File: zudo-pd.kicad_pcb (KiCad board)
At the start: 2 copper layers, 76 x 99 mm, 82 parts, among them J1 USB-C, J2 2541WR-2X08P, J3 2541WR-2X08P, J4 2541WR-2X08P, J5 2541WR-2X08P, J6 1217754-1, J7 1217754-1, J8 1217754-1, J9 1217754-1, U1 CH224D, U2 LM2596S-ADJ, U3 LM2596S-ADJ, U4 LM2596S-ADJ, U6 L7812CD2T-TR, U7 L7805ABD2T-TR, U8 CJ7912_C94173

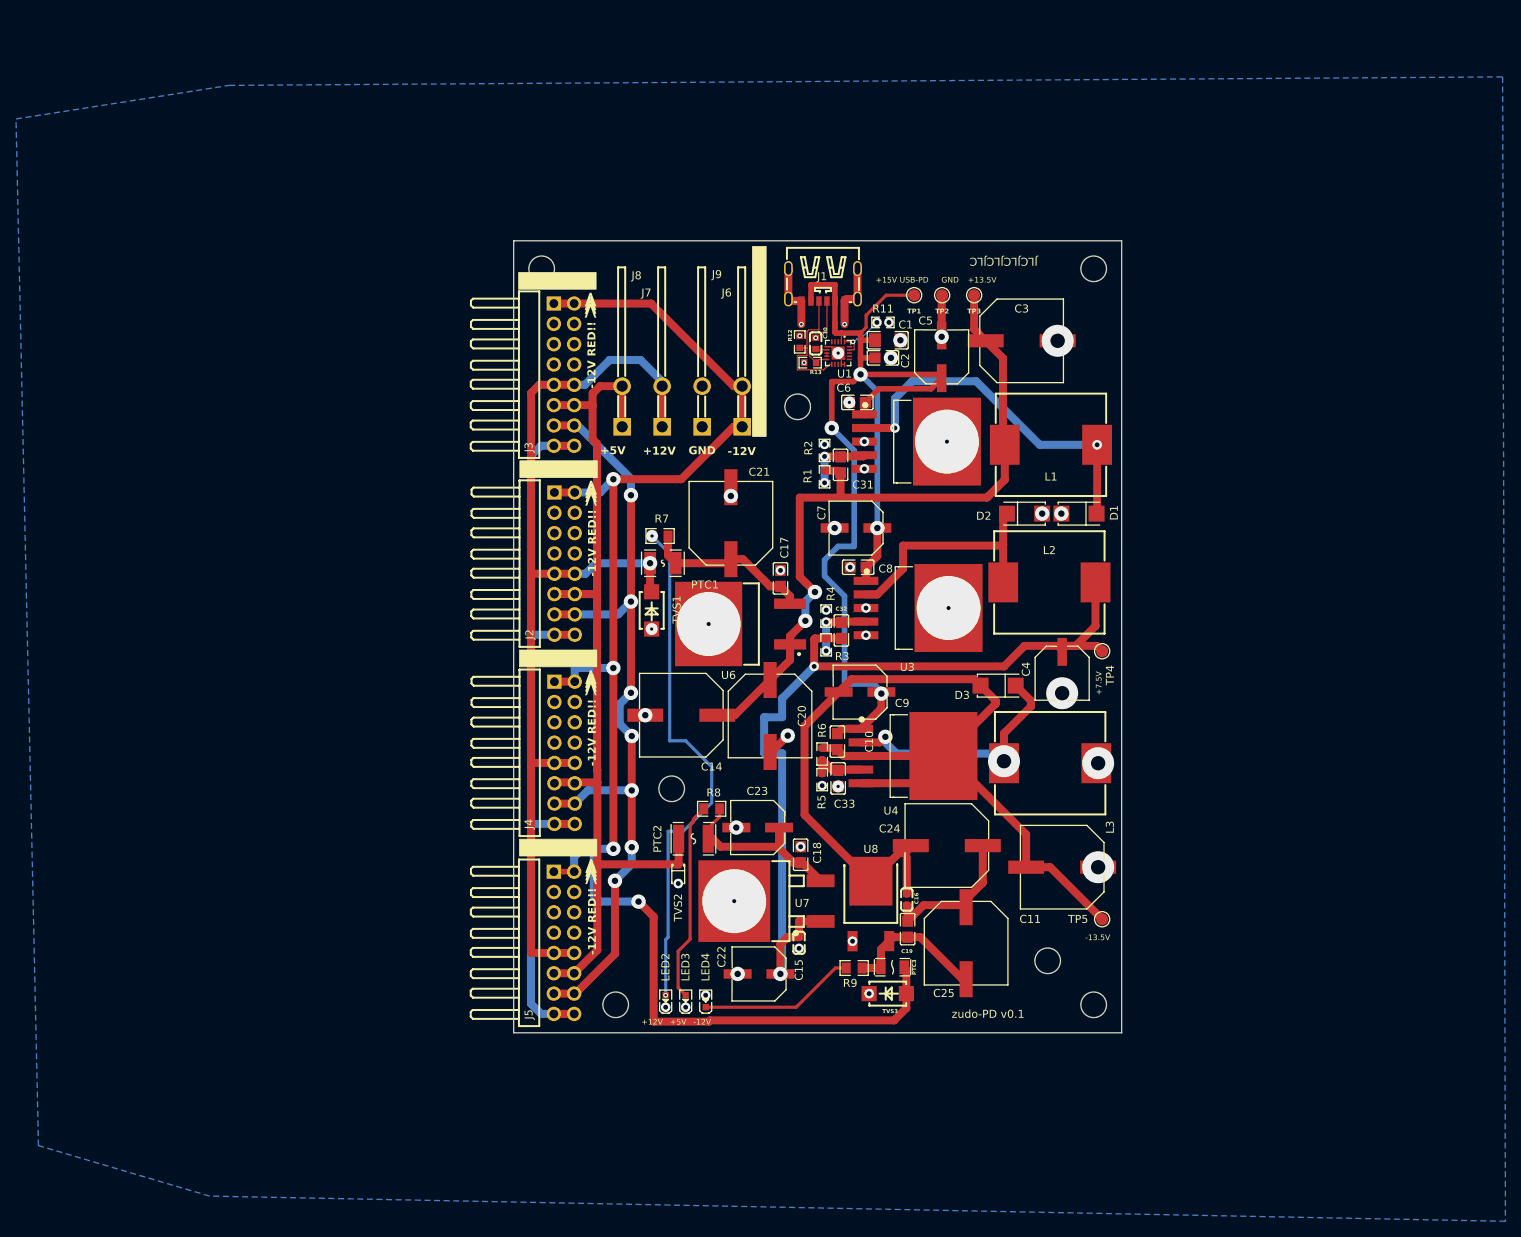
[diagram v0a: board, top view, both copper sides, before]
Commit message: Improve PCB layout for JLCPCB v1.1 production
- Fix via-in-pad issues for small passive components
- Add thermal via arrays under IC thermal pads
- Update trace widths to 0.7mm for 3A USB-PD input paths
- Adjust component placements and routing
- Remove unused output schematic elements

Co-Authored-By: Claude Opus 4.5 <noreply@anthropic.com>
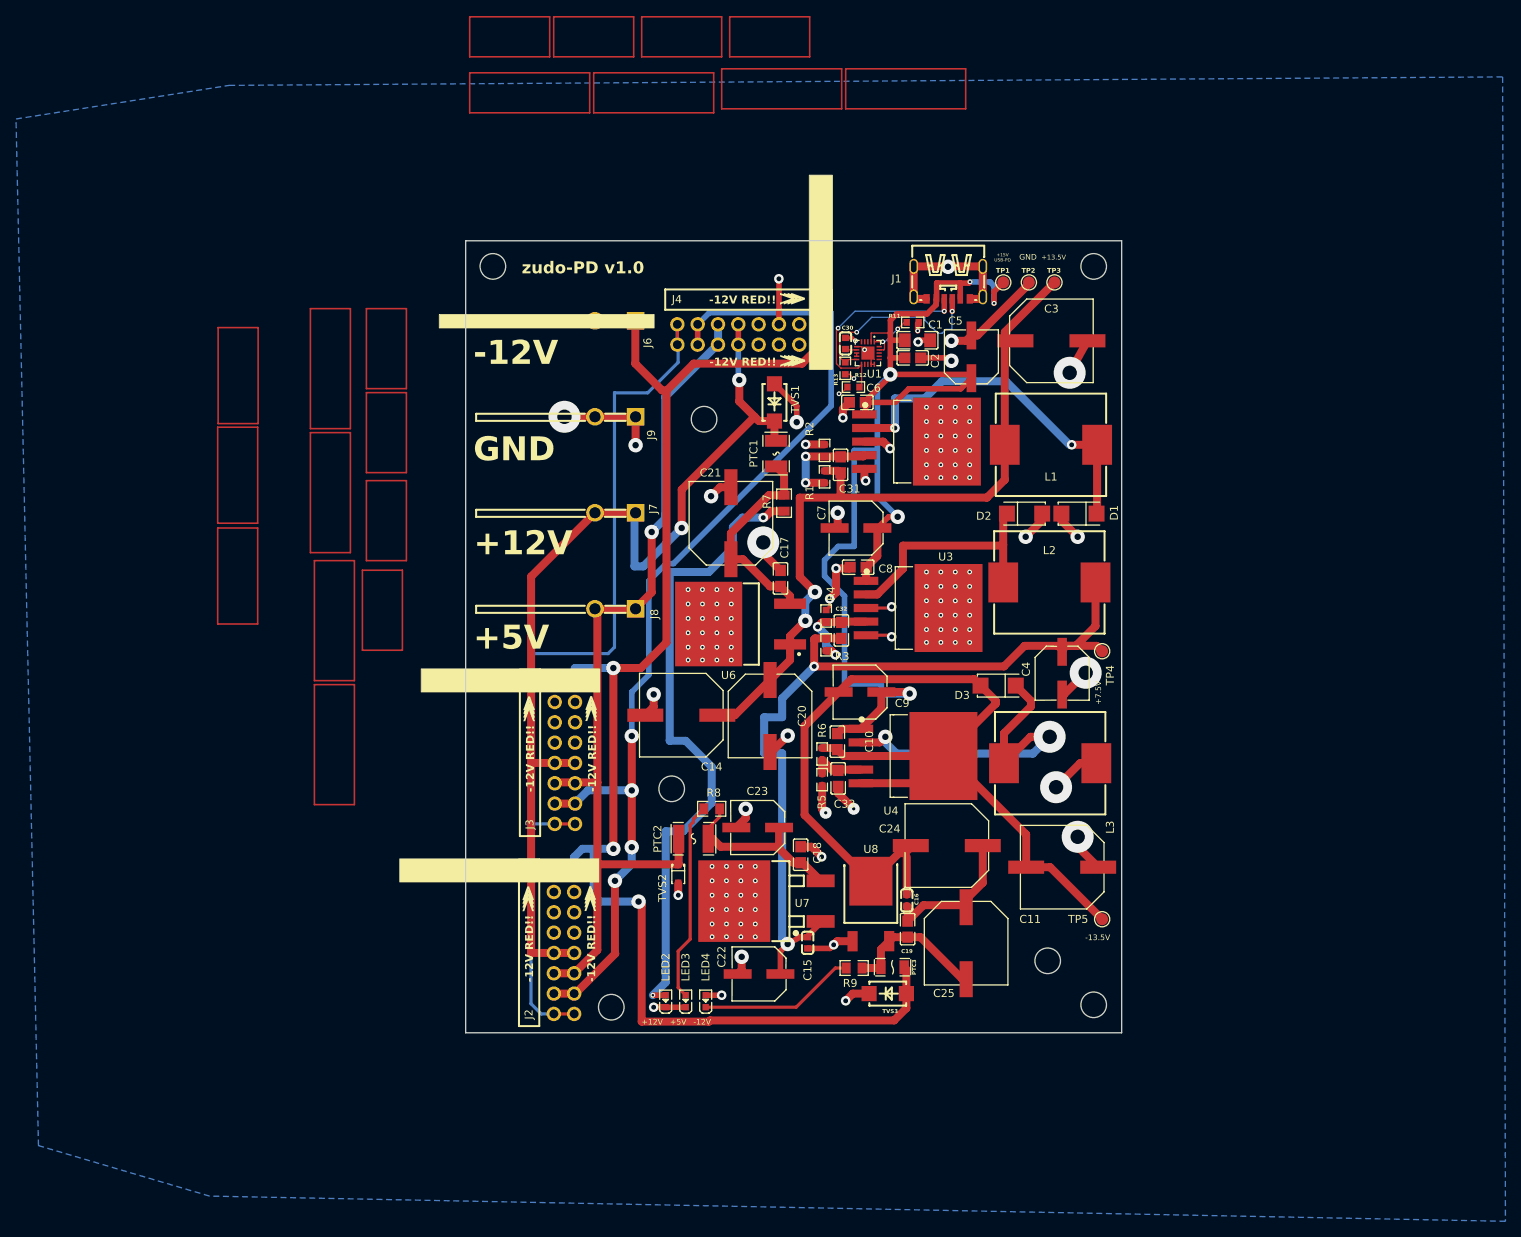
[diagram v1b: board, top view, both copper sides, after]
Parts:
- removed the J2 at (6.36, 40.4)
- removed the REF** at (12.8, 95.5)
- added ?: , , F.Cu at (12.2, 95.8)
- moved J4 57.1 mm to (29.4, 11.7), turned to 180 degrees
- moved J3 47.3 mm to (6.40, 64.0)
- moved TVS1 30.2 mm to (32.6, 20.2), turned to 90 degrees
- moved J8 25.3 mm to (12.7, 46.0), turned to -90 degrees
- moved PTC1 19.7 mm to (32.8, 26.6), turned to 90 degrees
- moved J6 19.1 mm to (12.7, 10.0), turned to -90 degrees
- moved R7 16.0 mm to (33.8, 32.8), turned to -90 degrees
- moved J1 15.7 mm to (54.3, 5.23)
- moved J7 14.5 mm to (12.7, 34.0), turned to -90 degrees
- moved REF** 11.8 mm to (23.8, 22.3)
- moved TP1 11.3 mm to (61.2, 5.20)
- moved TP2 11.0 mm to (64.4, 5.20)
- moved J9 10.9 mm to (12.7, 22.0), turned to -90 degrees
- moved TP3 10.2 mm to (67.6, 5.20)
- moved R12 8.78 mm to (42.5, 18.3), turned to 0 degrees
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- renumbered J5 to J2
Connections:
- net GND rail renamed GND
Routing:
- net GND: track 30.5 -> 172.8 mm, vias 46 -> 138
- net CV rail: track 104.6 -> 132.2 mm, vias 7 -> 4
- net GATE rail: track 91.4 -> 114.5 mm
- net Net-(LED2-A): track 65.1 -> 81.0 mm
- net Net-(J1-CC1): track 11.7 -> 25.4 mm, vias 0 -> 2
- net Net-(D3-K): track 32.3 -> 45.4 mm
- net +15V -> +13.5V gen: track 144.6 -> 156.3 mm, vias 4 -> 5
- net Net-(J1-CC2): track 16.7 -> 26.8 mm, vias 0 -> 2
- net /DC-DC Conversion/+7.5V OUT: track 111.4 -> 105.8 mm
- net Net-(U6-OUT): track 21.2 -> 26.2 mm
- net Net-(U2-Feedback): track 8.34 -> 13.1 mm
- net Net-(U3-Feedback): track 8.64 -> 12.1 mm
- net -12V rail: track 190.0 -> 186.6 mm, vias 4 -> 3
- net /DC-DC Conversion/+13.5V OUT: track 91.7 -> 94.6 mm
- net +5V rail: track 114.7 -> 113.0 mm, vias 0 -> 1
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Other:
- board size 76 x 99 mm -> 82 x 99 mm
- board text added: "< 6mm > pin legth"
- board text added: "zudo-PD v1.0"
- board text removed: "-12V RED!!"
- board text removed: ">"
- board text removed: "JLCJLCJLCJLC"
- board text removed: "zudo-PD v0.1"

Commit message: feat: Update PCB layout with improved routing and net naming
- Sync schematic changes to PCB layout with USBLC6-2SC6 component
- Update output connector designators to J10, J11
- Refine net naming for better clarity
- Update position files output path in project settings

Co-Authored-By: Claude <noreply@anthropic.com>
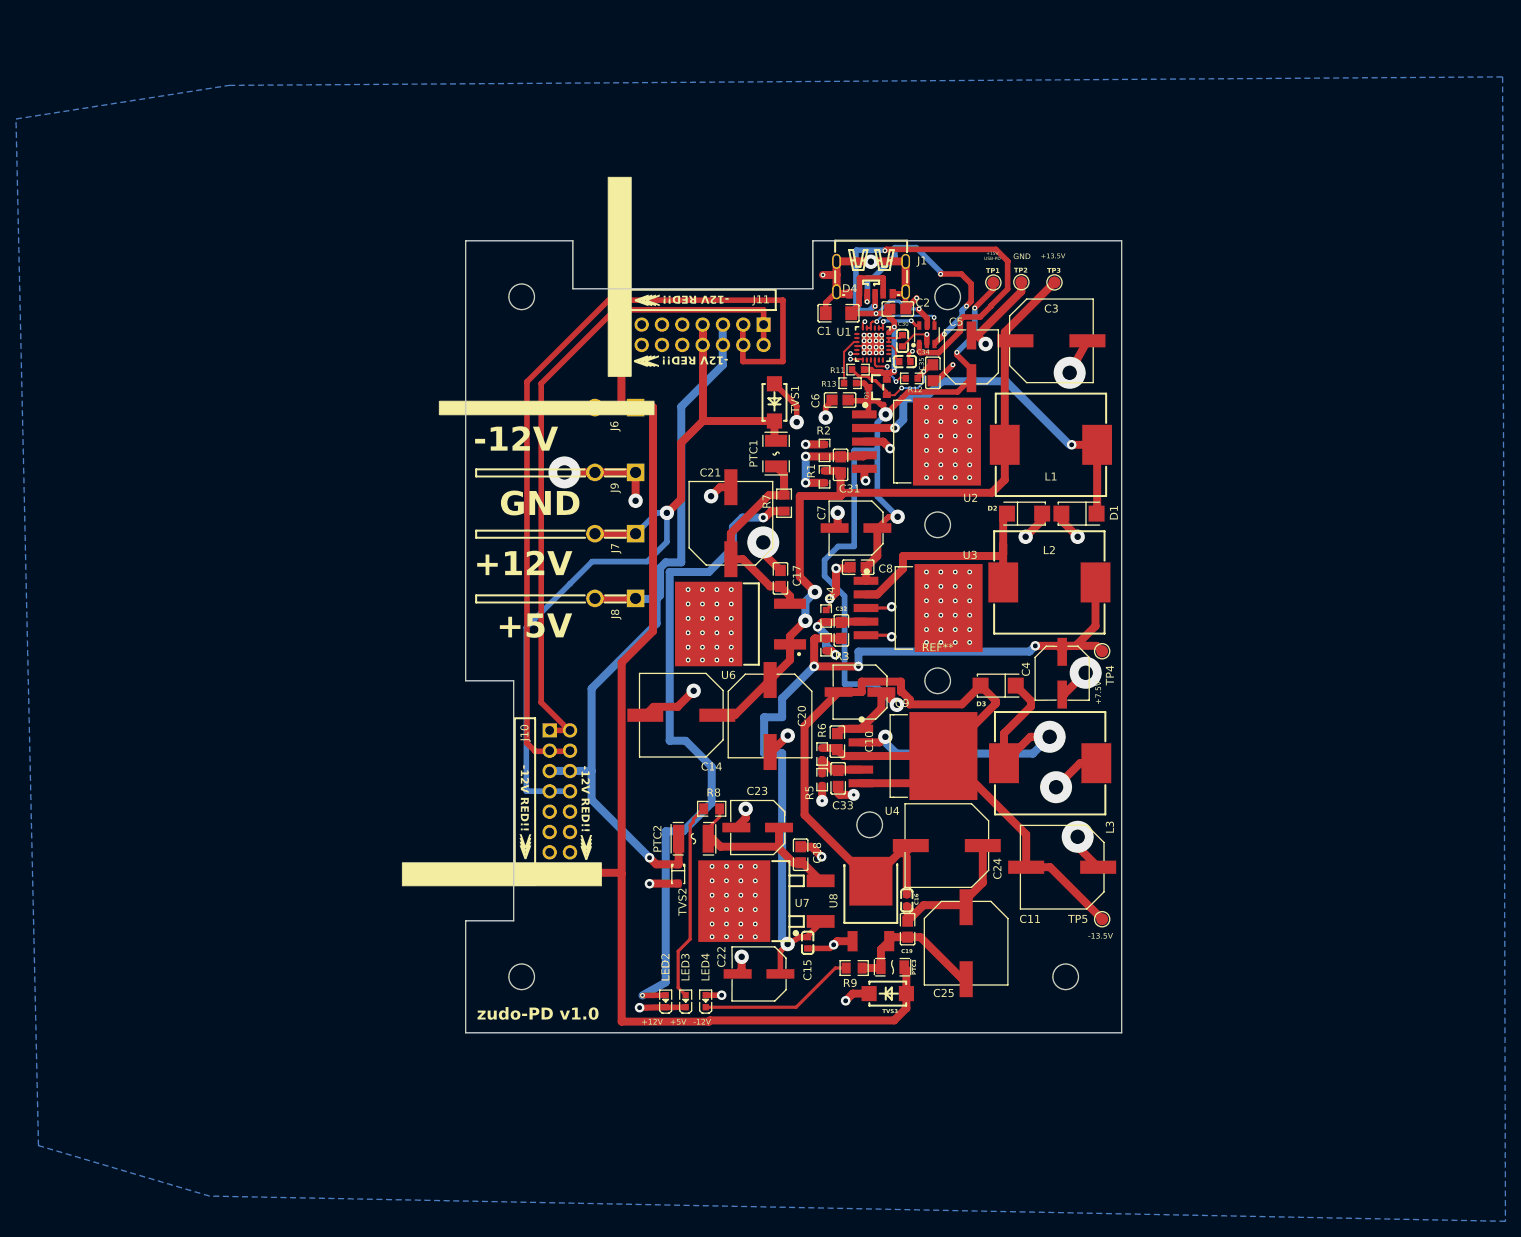
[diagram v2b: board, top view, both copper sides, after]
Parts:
- removed ?: , 
- removed J3, J4: 2541WR-2X08P, zudo-pd:HDR-TH_16P-P2.54-H-M-R2-C8-S2.54
- removed the REF** at (72.5, 3.20)
- removed the REF** at (-2.60, 3.20)
- removed the REF** at (23.8, 22.3)
- removed the REF** at (72.5, 95.5)
- removed the REF** at (66.8, 90.0)
- removed the REF** at (19.8, 68.5)
- added C34: 1uF 16V, zudo-pd:C0603, F.Cu at (48.9, 15.1)
- added C35: 100nF 50V, zudo-pd:C0805, F.Cu at (52.4, 16.5)
- added D4: USBLC6-2SC6, zudo-pd:SOT-23-6_L2.9-W1.6-P0.95-LS2.8-BL, F.Cu at (51.6, 11.8)
- added J11: 2541WR-2X08P, zudo-pd:HDR-TH_16P-P2.54-H-M-R2-C8-S2.54, F.Cu at (22.4, 11.7)
- added Q1: -30V -4A, zudo-pd:SOT-23_L2.9-W1.3-P1.90-LS2.4-BR, F.Cu at (45.5, 18.3)
- added REF**: MountingHole_3.2mm_M3, MountingHole:MountingHole_3.2mm_M3, F.Cu at (1.00, 92.0)
- added REF**: MountingHole_3.2mm_M3, MountingHole:MountingHole_3.2mm_M3, F.Cu at (54.2, 7.00)
- added REF**: MountingHole_3.2mm_M3, MountingHole:MountingHole_3.2mm_M3, F.Cu at (44.5, 73.0)
- added REF**: MountingHole_3.2mm_M3, MountingHole:MountingHole_3.2mm_M3, F.Cu at (1.00, 7.00)
- added REF**: MountingHole_3.2mm_M3, MountingHole:MountingHole_3.2mm_M3, F.Cu at (69.0, 92.0)
- added REF**: MountingHole_3.2mm_M3, MountingHole:MountingHole_3.2mm_M3, F.Cu at (53.0, 55.0)
- added REF**: MountingHole_3.2mm_M3, MountingHole:MountingHole_3.2mm_M3, F.Cu at (53.0, 35.5)
- C30: value 1uF -> 1uF 16V
- R11: value 56k -> 100k
- R12: value 5.1k -> 56k
- R13: value 5.1k -> 470
- U1: value CH224D -> STUSB4500QTR; footprint zudo-pd:QFN-20_L3.0-W3.0-P0.40-BL-EP1.7 -> zudo-pd:QFN-24_L4.0-W4.0-P0.50-BL-EP2.8
- moved J10 17.7 mm to (5.77, 70.1)
- moved J6 10.9 mm to (12.7, 20.9)
- moved C1 10.4 mm to (40.6, 9.05), turned to 0 degrees
- moved J1 9.66 mm to (44.7, 4.60)
- moved R11 9.02 mm to (43.0, 16.1)
- moved R12 7.36 mm to (49.8, 17.2)
- moved C30 7.13 mm to (48.6, 12.5), turned to -90 degrees
- moved J9 6.95 mm to (12.7, 28.9)
- moved C2 6.39 mm to (48.0, 8.52)
- moved J7 2.61 mm to (12.7, 36.6)
- moved C6 2.18 mm to (40.8, 19.9)
- moved R13 1.95 mm to (42.0, 17.8), turned to 180 degrees
- moved J8 1.30 mm to (12.7, 44.7)
- moved U1 1.29 mm to (44.9, 12.9)
- moved TP1 1.24 mm to (60.0, 5.22)
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- renumbered J2 to J10
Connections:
- C1 pad 1: GND -> GND rail
- C1 pad 2: +15V -> +13.5V gen -> VBUS_IN
- C11 pad 1: GND -> GND rail
- C14 pad 2: GND -> GND rail
- C15 pad 2: GND -> GND rail
- C17 pad 1: GND -> GND rail
- C18 pad 2: GND -> GND rail
- C2 pad 1: GND -> GND rail
- C2 pad 2: +15V -> +13.5V gen -> VBUS_IN
- C20 pad 2: GND -> GND rail
- C21 pad 2: GND -> GND rail
- C22 pad 2: GND -> GND rail
- C23 pad 2: GND -> GND rail
- C3 pad 2: GND -> GND rail
- C30 pad 1: Net-(U1-VDD) -> Net-(U1-VREG_2V7)
- C30 pad 2: GND -> GND rail
- C33 pad 1: GND -> GND rail
- C4 pad 2: GND -> GND rail
- C5 pad 2: GND -> GND rail
- C6 pad 2: GND -> GND rail
- C7 pad 2: GND -> GND rail
- C8 pad 2: GND -> GND rail
- D1 pad 2: GND -> GND rail
- D2 pad 2: GND -> GND rail
- J1 pad 7: GND -> GND rail
- J1 pad A12: GND -> GND rail
- J1 pad A9: +15V -> +13.5V gen -> VBUS_IN
- J1 pad B12: GND -> GND rail
- J1 pad B9: +15V -> +13.5V gen -> VBUS_IN
- J10 pad 1: -12V rail -> GATE rail
- J10 pad 10: +12V rail -> GND rail
- J10 pad 11: +5V rail -> GND rail
- J10 pad 12: +5V rail -> GND rail
- J10 pad 13: CV rail -> GND rail
- J10 pad 14: CV rail -> GND rail
- J10 pad 15: GATE rail -> -12V rail
- J10 pad 16: GATE rail -> -12V rail
- J10 pad 2: -12V rail -> GATE rail
- J10 pad 3: GND -> CV rail
- J10 pad 4: GND -> CV rail
- J10 pad 5: GND -> +5V rail
- J10 pad 6: GND -> +5V rail
- J10 pad 7: GND -> +12V rail
- J10 pad 8: GND -> +12V rail
- J10 pad 9: +12V rail -> GND rail
- J9 pad 1: GND -> GND rail
- J9 pad 2: GND -> GND rail
- L3 pad 2: GND -> GND rail
- LED2 pad 1: GND -> GND rail
- LED3 pad 1: GND -> GND rail
- LED4 pad 2: GND -> GND rail
- R11 pad 1: Net-(U1-CFG1) -> Net-(Q1-G)
- R11 pad 2: GND -> VBUS_IN
- R12 pad 1: GND -> Net-(U1-VBUS_EN_SNK)
- R12 pad 2: Net-(J1-CC2) -> Net-(Q1-G)
- R13 pad 1: GND -> +15V -> +13.5V gen
- R13 pad 2: Net-(J1-CC1) -> Net-(U1-DISCH)
- R2 pad 1: GND -> GND rail
- R4 pad 2: GND -> GND rail
- R5 pad 2: GND -> GND rail
- TP2 pad 1: GND -> GND rail
- TVS1 pad 2: GND -> GND rail
- TVS2 pad 1: GND -> GND rail
- TVS3 pad 1: GND -> GND rail
- U1 pad 1: Net-(U1-CFG1) -> Net-(U1-CC1)
- U1 pad 10: Net-(J1-CC1) -> GND rail
- U1 pad 11: Net-(J1-CC2) -> unconnected-(U1-ATTACH-Pad11)
- U1 pad 12: unconnected-(U1-CFG3-Pad12) -> GND rail
- U1 pad 13: unconnected-(U1-CFG2-Pad13) -> GND rail
- U1 pad 14: GND -> unconnected-(U1-POWER_OK3-Pad14)
- U1 pad 15: GND -> unconnected-(U1-GPIO-Pad15)
- U1 pad 16: unconnected-(U1-NC-Pad16) -> Net-(U1-VBUS_EN_SNK)
- U1 pad 19: Net-(U1-CFG1) -> unconnected-(U1-ALERT-Pad19)
- U1 pad 2: +15V -> +13.5V gen -> Net-(U1-CC1)
- U1 pad 21: GND -> Net-(U1-VREG_1V2)
- U1 pad 4: unconnected-(U1-NC-Pad4) -> Net-(U1-CC2)
- U1 pad 5: unconnected-(U1-GATE-Pad5) -> Net-(U1-CC2)
- U1 pad 6: GND -> GND rail
- U1 pad 7: Net-(U1-VDD) -> unconnected-(U1-SCL-Pad7)
- U1 pad 8: Net-(U1-DM) -> unconnected-(U1-SDA-Pad8)
- U1 pad 9: Net-(U1-DM) -> Net-(U1-DISCH)
- U2 pad 3: GND -> GND rail
- U2 pad 5: GND -> GND rail
- U2 pad 6: GND -> GND rail
- U3 pad 3: GND -> GND rail
- U3 pad 5: GND -> GND rail
- U3 pad 6: GND -> GND rail
- U6 pad 4: GND -> GND rail
- U7 pad 2: GND -> GND rail
- U8 pad 1: GND -> GND rail
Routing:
- net GND rail: track 0.00 -> 181.2 mm, vias 0 -> 154
- net GND: track 172.8 -> 0.00 mm, vias 138 -> 0
- net +15V -> +13.5V gen: track 156.3 -> 117.2 mm
- net VBUS_IN: track 0.00 -> 37.4 mm, vias 0 -> 4
- net -12V rail: track 186.6 -> 150.7 mm, vias 3 -> 0
- net GATE rail: track 114.5 -> 83.5 mm
- net CV rail: track 132.2 -> 104.6 mm, vias 4 -> 0
- net Net-(J1-CC1): track 25.4 -> 50.9 mm
- net +12V rail: track 124.5 -> 104.3 mm, vias 2 -> 1
- net Net-(Q1-G): track 0.00 -> 15.2 mm, vias 0 -> 2
- net Net-(U1-CC2): track 0.00 -> 10.8 mm, vias 0 -> 2
- net +5V rail: track 113.0 -> 103.4 mm
- net Net-(U1-CFG1): track 6.91 -> 0.00 mm, vias 2 -> 0
- net Net-(U1-CC1): track 0.00 -> 6.59 mm, vias 0 -> 2
- net Net-(U1-DISCH): track 0.00 -> 6.03 mm
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- added copper zone on B.Cu, net GND rail
- removed copper zone on B.Cu, net GND
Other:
- outline, holes or cut-outs redrawn
